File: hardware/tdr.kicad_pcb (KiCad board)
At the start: 2 copper layers, 190 parts, among them J201 Conn_02x01, J202 Conn_Coaxial, J203 Conn_Coaxial, J204 Conn_Coaxial, J205 Conn_Coaxial, J206 Conn_Coaxial, J207 Conn_Coaxial, J208 Conn_Coaxial, J209 Conn_Coaxial, J210 Barrel_Jack_Switch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

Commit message: work on schematic..
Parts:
- removed C203, C204, C208, C210: 2.2 uF, Capacitors_SMD:C_0603
- removed R206: TBD, Resistors_SMD:R_0402
- removed R701: R_Small, Resistors_SMD:R_0402
- removed U202, U204: LD39100, Housings_DFN_QFN:DFN-6-1EP_3x3mm_Pitch0.95mm
- added C801: 33 pF, Capacitors_SMD:C_0402, F.Cu at (215.2, 101.5)
- added C802: 1 uF, Capacitors_SMD:C_0603, F.Cu at (199.6, 107.0)
- added C803: 33 pF, Capacitors_SMD:C_0402, F.Cu at (210.0, 104.6)
- added C804: 10 nF, Capacitors_SMD:C_0402, F.Cu at (210.0, 103.4)
- added C805: 33 pF, Capacitors_SMD:C_0402, F.Cu at (207.0, 106.0)
- added C806: 1 uF, Capacitors_SMD:C_0603, F.Cu at (203.2, 103.5)
- added C807: 33 pF, Capacitors_SMD:C_0402, F.Cu at (211.7, 105.9)
- added C808: 10 nF, Capacitors_SMD:C_0402, F.Cu at (217.5, 102.6)
- added C809: C_Small, Capacitors_SMD:C_0402, F.Cu at (214.7, 104.0)
- added C810: C_Small, Capacitors_SMD:C_0402, F.Cu at (219.6, 98.7)
- added C811: 33 pF, Capacitors_SMD:C_0402, F.Cu at (211.7, 107.1)
- added C812: 33 pF, Capacitors_SMD:C_0402, F.Cu at (217.5, 101.4)
- added C813: 33 pF, Capacitors_SMD:C_0402, F.Cu at (212.3, 104.6)
- added C814: 33 pF, Capacitors_SMD:C_0402, F.Cu at (209.4, 106.0)
- added C815: 33 pF, Capacitors_SMD:C_0402, F.Cu at (209.4, 107.3)
- added C816: 33 pF, Capacitors_SMD:C_0402, F.Cu at (219.3, 97.5)
- added C817: 33 pF, Capacitors_SMD:C_0402, F.Cu at (217.2, 100.1)
- added C818: 33 pF, Capacitors_SMD:C_0402, F.Cu at (207.0, 107.3)
- added C819: 33 pF, Capacitors_SMD:C_0402, F.Cu at (219.3, 96.2)
- added C820: 33 pF, Capacitors_SMD:C_0402, F.Cu at (217.2, 98.9)
- added C821: 33 pF, Capacitors_SMD:C_0402, F.Cu at (215.2, 102.8)
- added C822: 33 pF, Capacitors_SMD:C_0402, F.Cu at (212.3, 103.4)
- added J801: Conn_02x06_Odd_Even, Pin_Headers:Pin_Header_Angled_2x06, F.Cu at (95.0, 75.9)
- added J802: Conn_02x06_Odd_Even, Pin_Headers:Pin_Header_Angled_2x06, F.Cu at (95.0, 98.8)
- added L801: L_Small, Resistors_SMD:R_0402, F.Cu at (202.0, 107.6)
- added L802: L_Small, Resistors_SMD:R_0402, F.Cu at (214.5, 105.3)
- added Q201: SI2369DS, TO_SOT_Packages_SMD:SOT-23, F.Cu at (177.0, 99.3)
- added R236: DNP, Resistors_SMD:R_0402, F.Cu at (192.5, 87.6)
- added R237: DNP, Resistors_SMD:R_0402, F.Cu at (185.5, 94.4)
- added RN801: 22, Resistors_SMD:R_Array_Convex_4x0402, F.Cu at (217.1, 96.9)
- added RN802: 22, Resistors_SMD:R_Array_Convex_4x0402, F.Cu at (204.8, 106.7)
- added RN803: 22, Resistors_SMD:R_Array_Convex_4x0402, F.Cu at (207.8, 104.1)
- added RN804: 22, Resistors_SMD:R_Array_Convex_4x0402, F.Cu at (215.0, 99.6)
- added RN805: 22, Resistors_SMD:R_Array_Convex_4x0402, F.Cu at (215.0, 96.9)
- added RN806: 22, Resistors_SMD:R_Array_Convex_4x0402, F.Cu at (205.7, 104.1)
- added RN807: 22, Resistors_SMD:R_Array_Convex_4x0402, F.Cu at (202.8, 105.6)
- added TP801: TestPoint, vna_footprints:TP07R, F.Cu at (201.4, 106.6)
- added TP802: TestPoint, vna_footprints:TP07R, F.Cu at (204.1, 104.6)
- added TP803: TestPoint, vna_footprints:TP07R, F.Cu at (203.3, 107.3)
- added U801: 74HC244, Housings_SSOP:TSSOP-20_4.4x6.5mm_Pitch0.65mm, F.Cu at (210.0, 99.2)
- added U802: 74HC244, Housings_SSOP:TSSOP-20_4.4x6.5mm_Pitch0.65mm, F.Cu at (202.1, 99.2)
- added U803: 74xx1G14, TO_SOT_Packages_SMD:SOT-23-5, F.Cu at (199.9, 104.6)
- R202: value 10k -> JMP
- R204: value TBD -> JMP
- R207, R209, R210: value 10k -> DNP
- R213, R215: value TBD -> DNP
- moved U205 81.2 mm to (172.7, 103.0)
- moved R204 79.6 mm to (181.6, 95.8)
- moved R215 79.1 mm to (177.1, 104.3)
- moved R208 72.9 mm to (181.6, 98.5)
- moved C202 72.2 mm to (158.7, 103.4)
- moved R203 70.7 mm to (175.1, 101.6)
- moved C206 70.7 mm to (149.9, 103.4)
- moved R226 70.4 mm to (177.1, 101.6)
- moved R202 69.8 mm to (179.7, 98.3)
- moved C215 69.8 mm to (179.7, 84.5)
- moved J203 69.8 mm to (165.7, 97.5)
- moved J205 69.8 mm to (165.7, 102.6)
- moved D201 69.7 mm to (185.0, 91.6)
- moved R213 68.7 mm to (187.5, 92.8)
- moved R235 68.3 mm to (175.1, 104.3)
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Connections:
- net /conn_power/~PGOOD renamed /conn_power/~PGOOD_5V
- F201 pad 1: VPP -> Net-(F201-Pad1)
- R201 pad 1: Net-(R201-Pad1) -> VPP
- R201 pad 2: GND -> Net-(R201-Pad2)
- R202 pad 2: GND -> /PGOOD_3V3
- R204 pad 2: +2V5 -> /PGOOD_3V3
- R207 pad 1: Net-(R207-Pad1) -> VPP
- R207 pad 2: GND -> /PGOOD_3V3
- R208 pad 1: Net-(R208-Pad1) -> VPP
- R208 pad 2: GND -> /PGOOD_3V3
- R209 pad 1: Net-(R209-Pad1) -> Net-(R202-Pad1)
- R210 pad 1: Net-(R210-Pad1) -> Net-(R204-Pad1)
- R213 pad 1: Net-(R213-Pad1) -> Net-(J202-Pad1)
- R213 pad 2: +3.3VP -> GND
- R215 pad 2: Net-(R213-Pad1) -> Net-(J202-Pad1)
- R324 pad 2: (no net) -> /clock/CLK_FPGA
- RN601 pad 1: (no net) -> /fpga_connector/DELAY_~EN
- RN601 pad 2: (no net) -> /fpga_connector/DELAY_SLOAD
- RN601 pad 3: (no net) -> /fpga_connector/DELAY_SDIN
- RN601 pad 4: (no net) -> /fpga_connector/DELAY_SCLK
- RN701 pad 1: (no net) -> /fpga_connector/DAC_SDI
- RN701 pad 2: (no net) -> /fpga_connector/DAC_SCK
- RN701 pad 3: (no net) -> /fpga_connector/DAC_CS
- RN701 pad 4: (no net) -> /fpga_connector/DAC_~CLR
- RN701 pad 5: (no net) -> Net-(RN701-Pad5)
- U201 pad 1: Net-(R201-Pad1) -> Net-(R201-Pad2)
- U201 pad 3: /conn_power/PGOOD_2V5 -> /PGOOD_3V3
- U203 pad 1: Net-(R207-Pad1) -> /PGOOD_3V3
- U203 pad 3: /conn_power/PGOOD_2V5 -> (no net)
- U205 pad 12: Net-(R209-Pad1) -> Net-(R202-Pad1)
- U205 pad 8: Net-(R210-Pad1) -> Net-(R204-Pad1)
- U302 pad 2: (no net) -> /clock/CLK_SEL
- U304 pad 18: (no net) -> /fpga_connector/SEL0
- U304 pad 19: (no net) -> /fpga_connector/SEL1
- U402 pad 7: (no net) -> /COMPARATOR_OUTPUT
- U701 pad 5: Net-(R701-Pad2) -> Net-(RN701-Pad5)
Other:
- copper layers 2 -> 4
- rule pad_to_mask_clearance: 0.051 -> 0.025

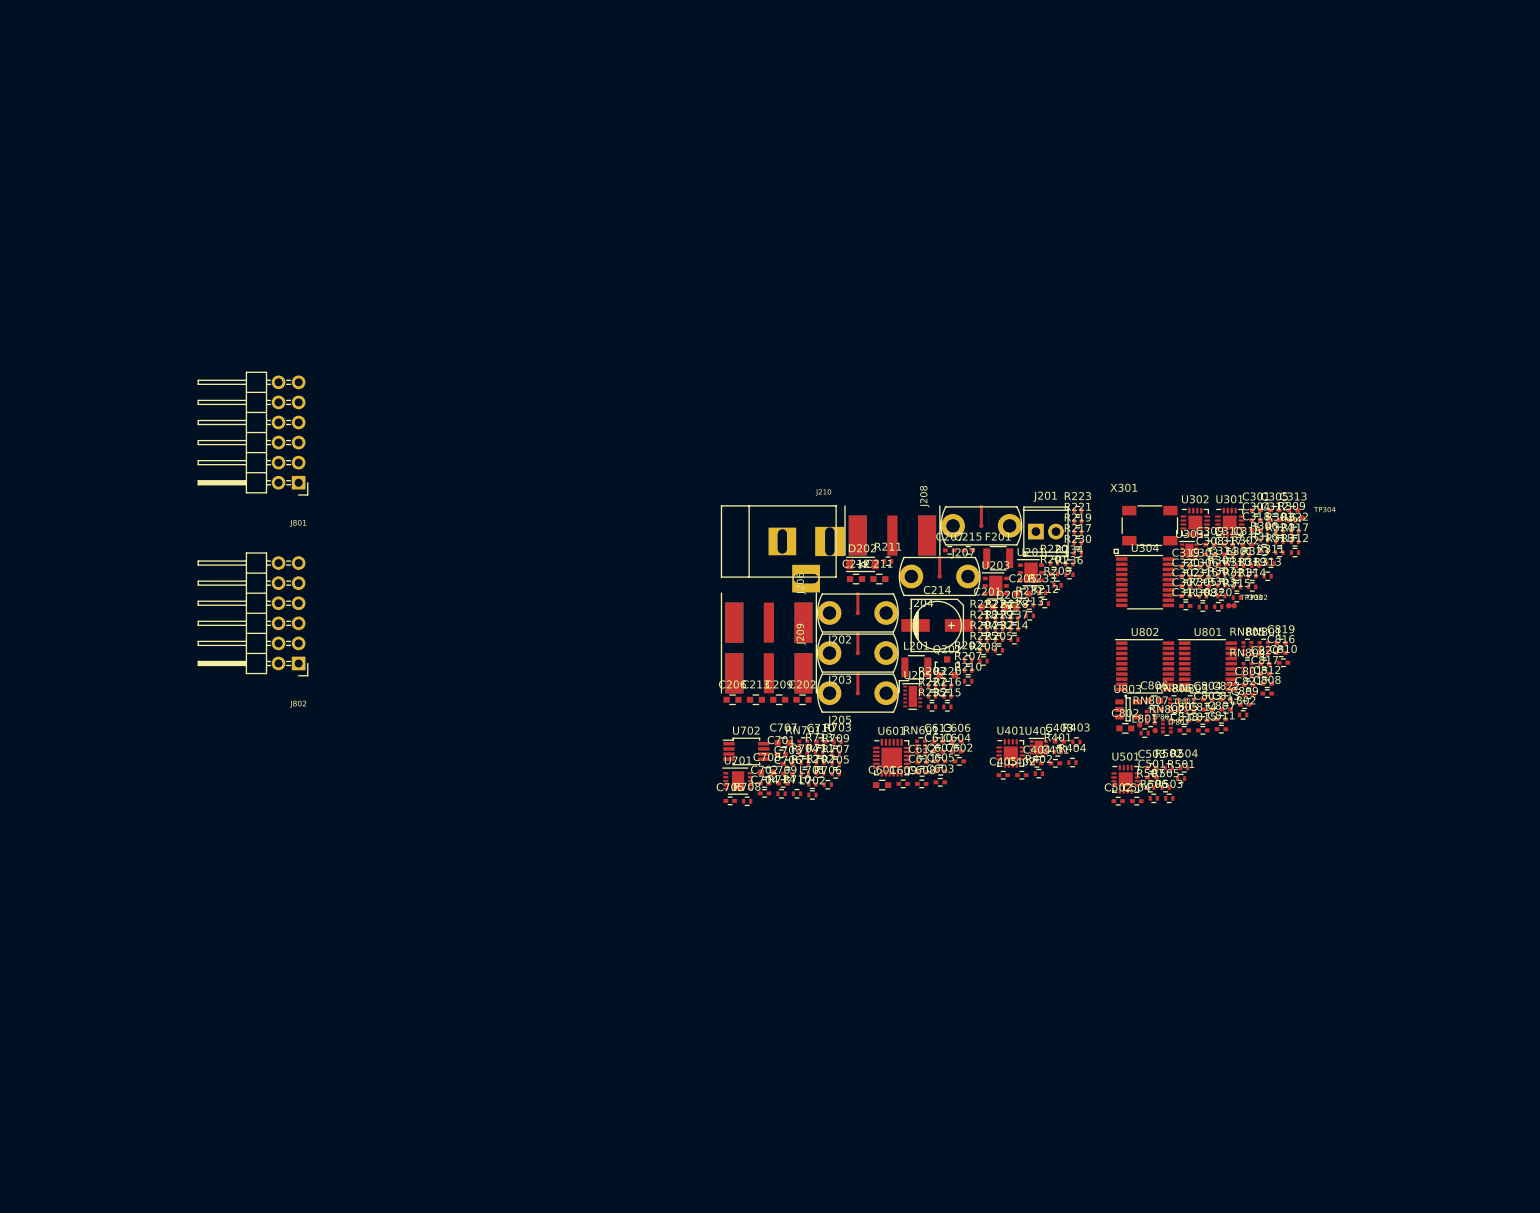
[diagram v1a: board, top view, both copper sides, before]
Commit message: work on tdr component placement
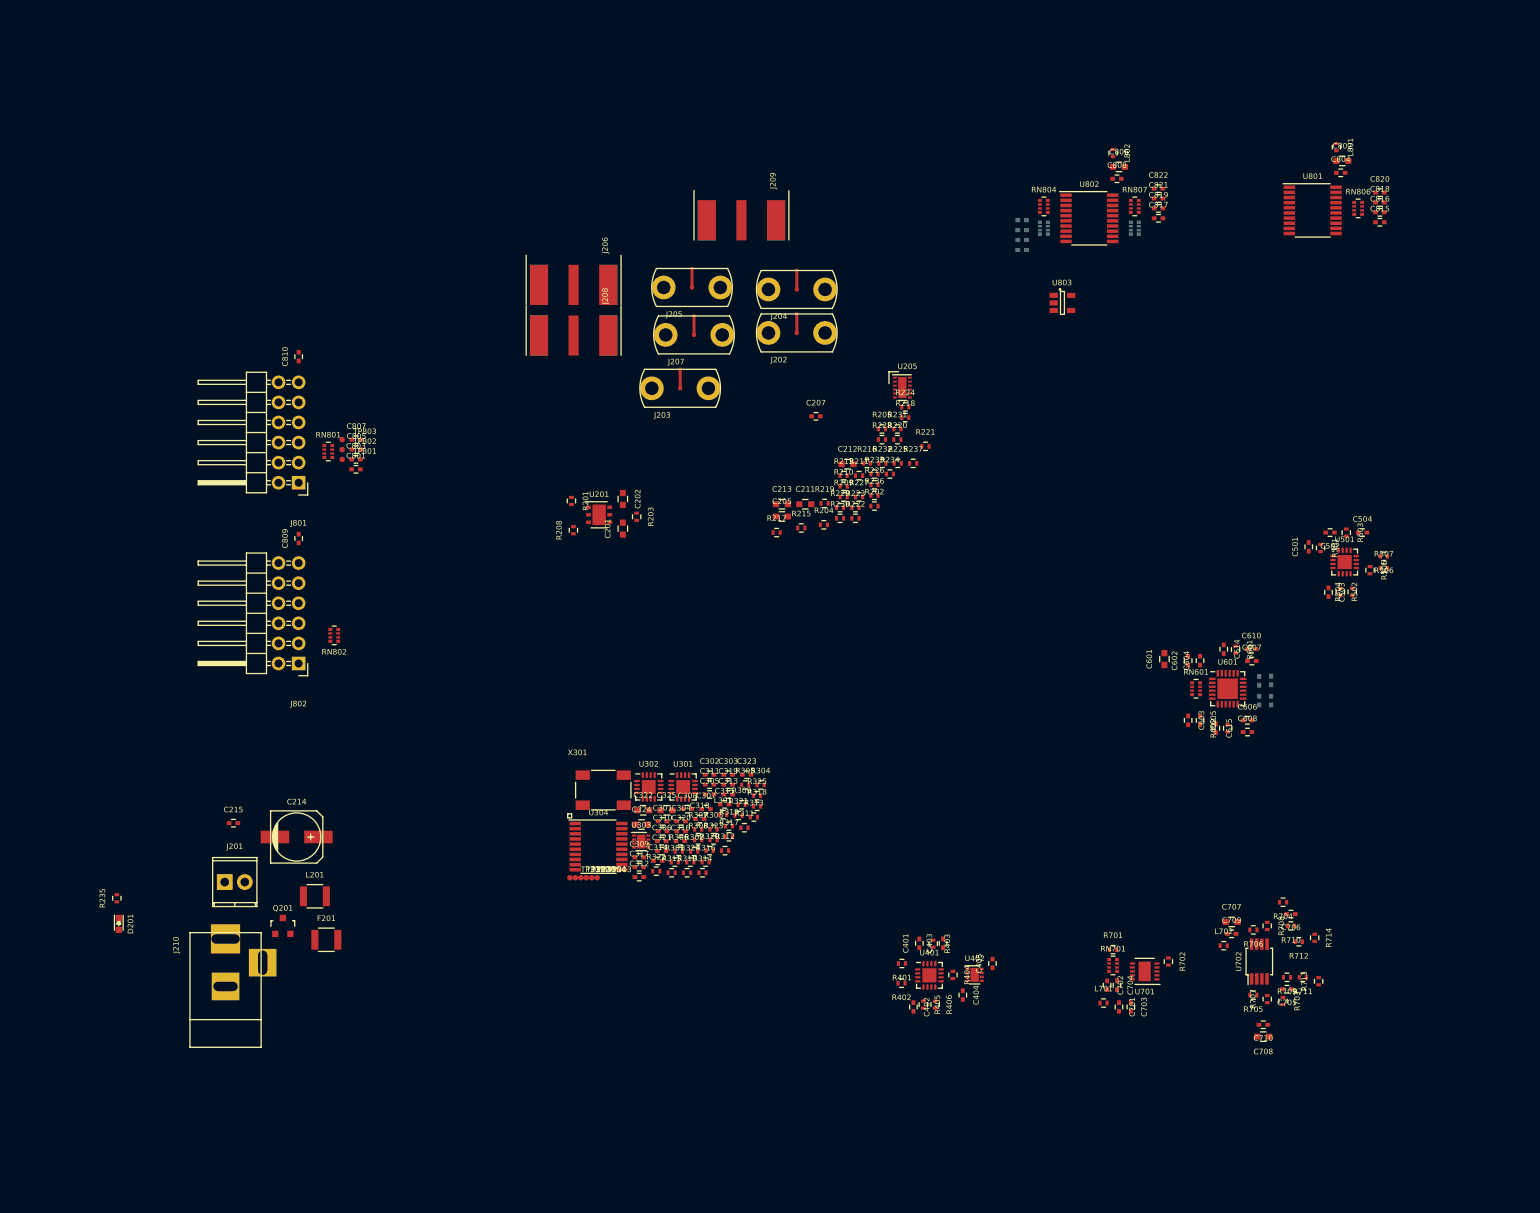
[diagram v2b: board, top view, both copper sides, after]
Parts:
- removed C206, C209: 2.2 uF, Capacitors_SMD:C_0603
- removed D202: TBD, Diodes_SMD:SOD-123
- removed R207: DNP, Resistors_SMD:R_0402
- removed R212, R214: TBD, Resistors_SMD:R_0402
- removed U203: LD39100, Housings_DFN_QFN:DFN-6-1EP_3x3mm_Pitch0.95mm
- added C321: 100 pF, Capacitors_SMD:C_0402, F.Cu at (140.9, 122.5)
- added C322: 2.2 uF, Capacitors_SMD:C_0603, F.Cu at (138.6, 117.4)
- added C323: 100 pF, Capacitors_SMD:C_0402, F.Cu at (151.7, 112.9)
- added C324: 2.2 uF, Capacitors_SMD:C_0603, F.Cu at (138.4, 119.2)
- added C325: 2.2 uF, Capacitors_SMD:C_0603, F.Cu at (141.5, 117.4)
- added C614: 10 nF, Capacitors_SMD:C_0402, F.Cu at (212.0, 97.0)
- added C615: 10 nF, Capacitors_SMD:C_0402, F.Cu at (211.0, 107.0)
- added R325: 125, Resistors_SMD:R_0402, F.Cu at (153.0, 115.5)
- added R405: JMP, Resistors_SMD:R_0402, F.Cu at (174.0, 141.9)
- added R406: JMP, Resistors_SMD:R_0402, F.Cu at (175.5, 141.9)
- added R601: 68, Resistors_SMD:R_0402, F.Cu at (213.5, 97.0)
- added R602: 68, Resistors_SMD:R_0402, F.Cu at (212.5, 107.0)
- added R701: 10k, Resistors_SMD:R_0402, F.Cu at (198.0, 135.0)
- added TP305: TestPoint, vna_footprints:TP07R, F.Cu at (131.4, 125.9)
- added TP306: TestPoint, vna_footprints:TP07R, F.Cu at (130.7, 125.9)
- C301, C303: value .01 uF -> 10 nF
- C609, C611, C612, C613, C811, C812, C813, C814, RN803, RN805: moved to B.Cu
- C801: value 33 pF -> 10 pF
- R321: value 50 -> 125
- R322: value 50 -> 84
- R323: value 68 -> 84
- moved C810 130.4 mm to (95.0, 60.0), turned to 90 degrees
- moved C809 121.5 mm to (95.0, 83.0), turned to 90 degrees
- moved RN801 120.9 mm to (98.8, 72.0)
- moved D201 119.7 mm to (72.2, 131.8), turned to 270 degrees
- moved C801 116.2 mm to (102.2, 74.2)
- moved C807 115.0 mm to (102.3, 70.5)
- moved C803 112.2 mm to (102.2, 73.0)
- moved J201 111.8 mm to (85.7, 126.5)
- moved C805 110.2 mm to (102.3, 71.8)
- moved TP803 109.2 mm to (100.5, 70.5)
- moved TP802 108.7 mm to (100.5, 71.8)
- moved TP801 106.3 mm to (100.5, 73.0)
- moved RN802 105.9 mm to (99.5, 95.2), turned to 180 degrees
- moved R235 105.9 mm to (72.0, 128.5), turned to 90 degrees
- moved TP304 100.7 mm to (132.1, 125.9)
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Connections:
- R321 pad 1: Net-(R321-Pad1) -> +3V3
- R322 pad 1: Net-(R321-Pad2) -> Net-(R322-Pad1)
- R322 pad 2: Net-(R322-Pad2) -> GND
- RN701 pad 1: /fpga_connector/DAC_SDI -> /fpga_connector/DAC_~CLR
- RN701 pad 2: /fpga_connector/DAC_SCK -> /fpga_connector/DAC_CS
- RN701 pad 3: /fpga_connector/DAC_CS -> /fpga_connector/DAC_SCK
- RN701 pad 4: /fpga_connector/DAC_~CLR -> /fpga_connector/DAC_SDI
- RN701 pad 8: Net-(RN701-Pad8) -> Net-(R701-Pad2)
- RN801 pad 1: Net-(J801-Pad1) -> Net-(J801-Pad7)
- RN801 pad 2: Net-(J801-Pad3) -> Net-(J801-Pad5)
- RN801 pad 3: Net-(J801-Pad5) -> Net-(J801-Pad3)
- RN801 pad 4: Net-(J801-Pad7) -> Net-(J801-Pad1)
- RN801 pad 5: Net-(C807-Pad1) -> /clock/CLK_FPGA
- RN801 pad 6: Net-(C805-Pad1) -> Net-(C803-Pad1)
- RN801 pad 7: Net-(C803-Pad1) -> Net-(C805-Pad1)
- RN801 pad 8: /clock/CLK_FPGA -> Net-(C807-Pad1)
- U302 pad 10: Net-(R322-Pad2) -> Net-(R322-Pad1)
- U302 pad 11: (no net) -> Net-(TP305-Pad1)
- U302 pad 12: (no net) -> Net-(TP306-Pad1)
- U302 pad 9: Net-(R321-Pad1) -> Net-(R321-Pad2)
- U303 pad 2: Net-(R321-Pad1) -> Net-(R321-Pad2)
- U303 pad 3: Net-(R322-Pad2) -> Net-(R322-Pad1)
- U401 pad 6: /delay_pulse/~DELAY1_OUT -> Net-(R405-Pad1)
- U401 pad 7: /delay_pulse/DELAY1_OUT -> Net-(R406-Pad1)
- U601 pad 10: +1V35 -> Net-(C615-Pad1)
- U601 pad 21: +1V35 -> Net-(C614-Pad2)
- U601 pad 24: +1V35 -> Net-(C614-Pad2)
- U601 pad 7: +1V35 -> Net-(C615-Pad1)
- U701 pad 5: Net-(RN701-Pad5) -> Net-(R701-Pad2)
- U701 pad 6: Net-(RN701-Pad6) -> Net-(RN701-Pad7)
- U701 pad 7: Net-(RN701-Pad7) -> Net-(RN701-Pad6)
- U701 pad 8: Net-(RN701-Pad8) -> Net-(RN701-Pad5)
